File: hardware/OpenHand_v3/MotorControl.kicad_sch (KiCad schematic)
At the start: 34 parts, among them U10 DRV8833PWP, U7 DRV8833PWP, U8 DRV8833PWP, U9 DRV8833PWP

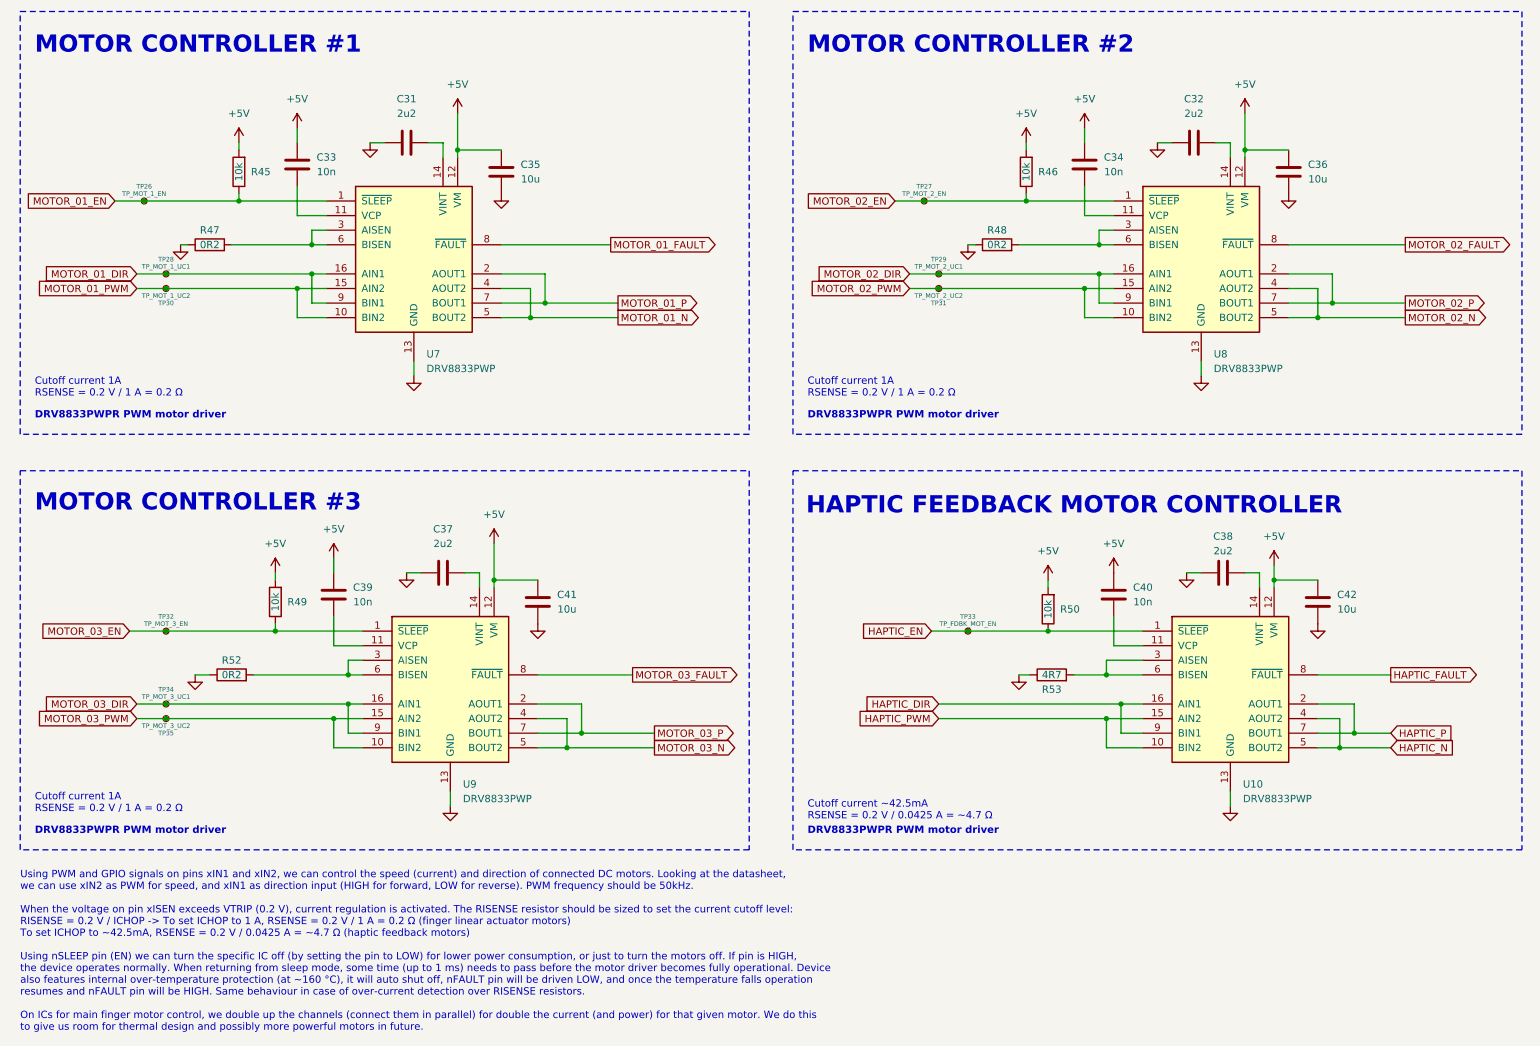
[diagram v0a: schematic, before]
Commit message: Finalize board v3, prepare CubeIDE config
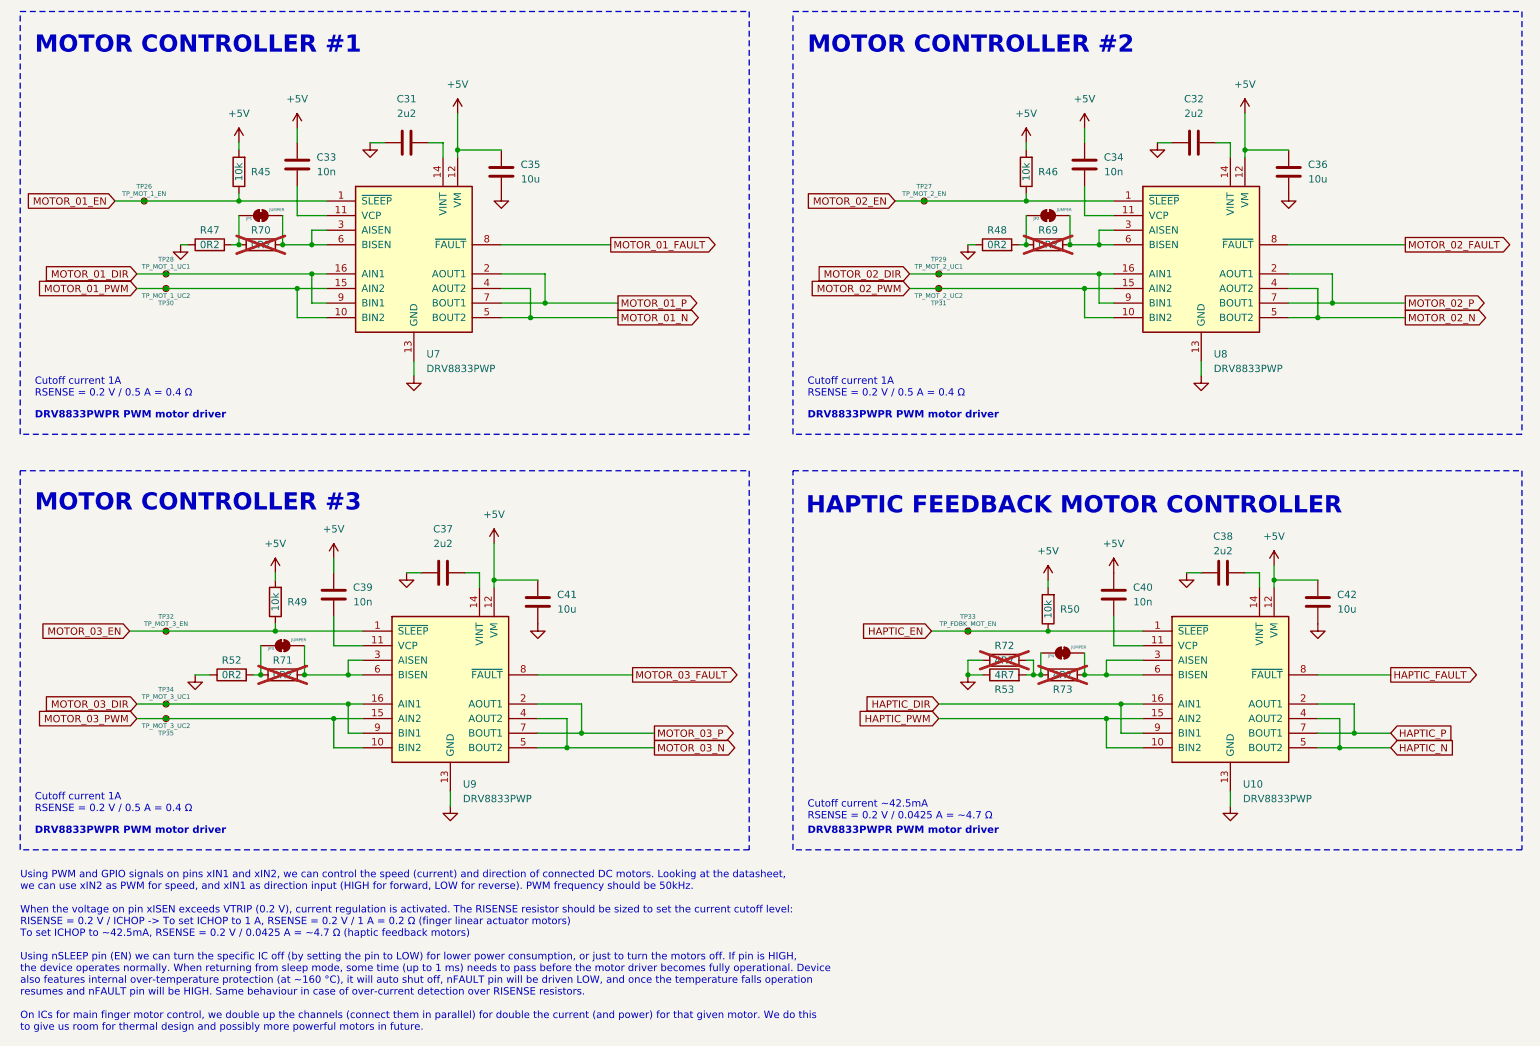
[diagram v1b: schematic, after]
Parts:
- added JP1, JP2, JP3, JP4: JUMPER, Jumper:SolderJumper-2_P1.3mm_Bridged_RoundedPad1.0x1.5mm, symbol Jumper:SolderJumper_2_Bridged
- added R69, R70, R71: 0R2, Resistor_SMD:R_1206_3216Metric, symbol Device:R
- added R72, R73: 4R7, Resistor_SMD:R_1206_3216Metric, symbol Device:R
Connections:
- net GND: now also R72.2
- net at U8.3 (AISEN), U8.6 (BISEN): now also JP2.2 (B), R69.2; no longer R48.2
- net at U9.3 (AISEN), U9.6 (BISEN): now also JP3.2 (B), R71.2; no longer R52.2
- net at U7.3 (AISEN), U7.6 (BISEN): now also JP1.2 (B), R70.2; no longer R47.2
- net at U10.3 (AISEN), U10.6 (BISEN): now also JP4.2 (B), R73.2; no longer R53.2
- new net: JP4.1 (A), R53.2, R72.1, R73.1
- new net: JP3.1 (A), R52.2, R71.1
- new net: JP2.1 (A), R48.2, R69.1
- new net: JP1.1 (A), R47.2, R70.1
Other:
- note added: "Cutoff current 1A RSENSE = 0.2 V / 0.5 A = 0.4 Ω"
- note removed: "Cutoff current 1A RSENSE = 0.2 V / 1 A = 0.2 Ω"
- moved on the sheet: R53
